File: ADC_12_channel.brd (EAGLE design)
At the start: 148.1 x 127 mm, 165 parts, among them IC1 LM317BD2T, IC2 LM317BD2T, K1 691131710003, K2 691101710002, K3 691101710002, K4 691101710002, K5 691101710002, K6 691101710002, K7 691101710002, K8 691101710002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

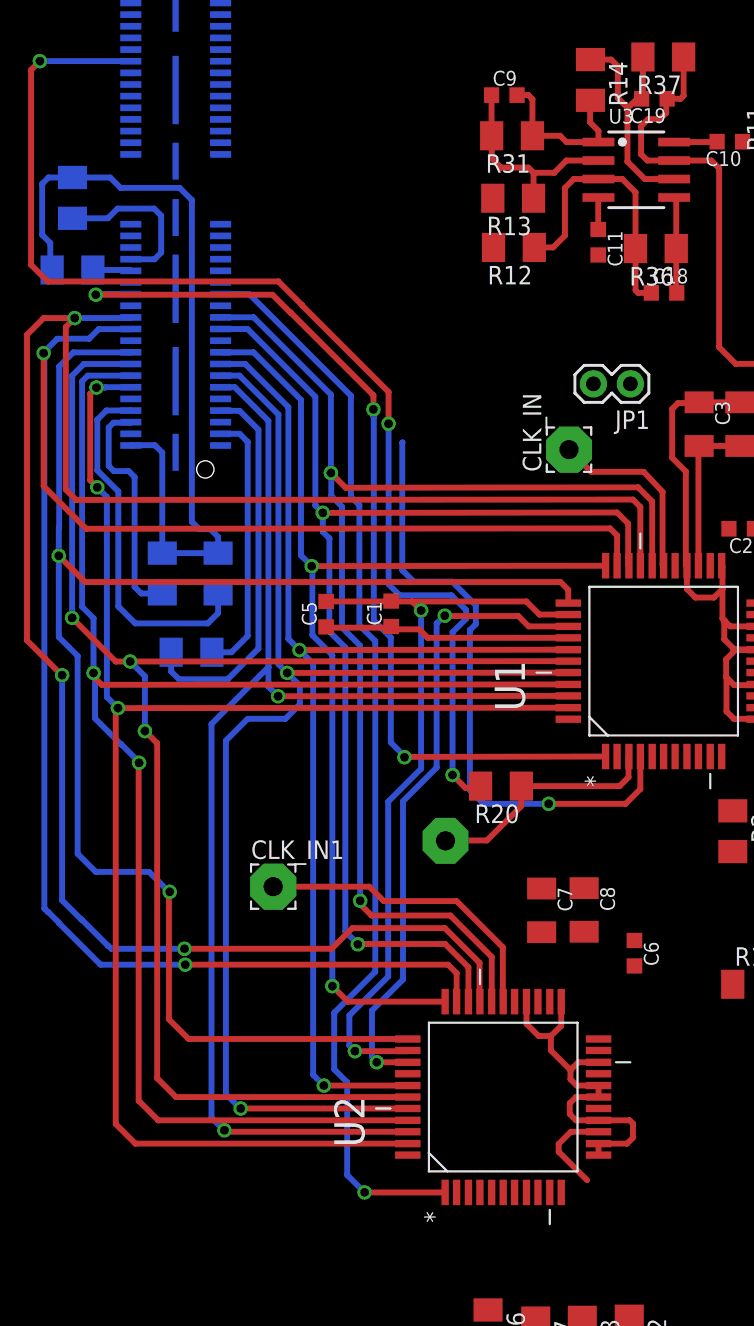
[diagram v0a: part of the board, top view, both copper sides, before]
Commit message: Finished connections to header
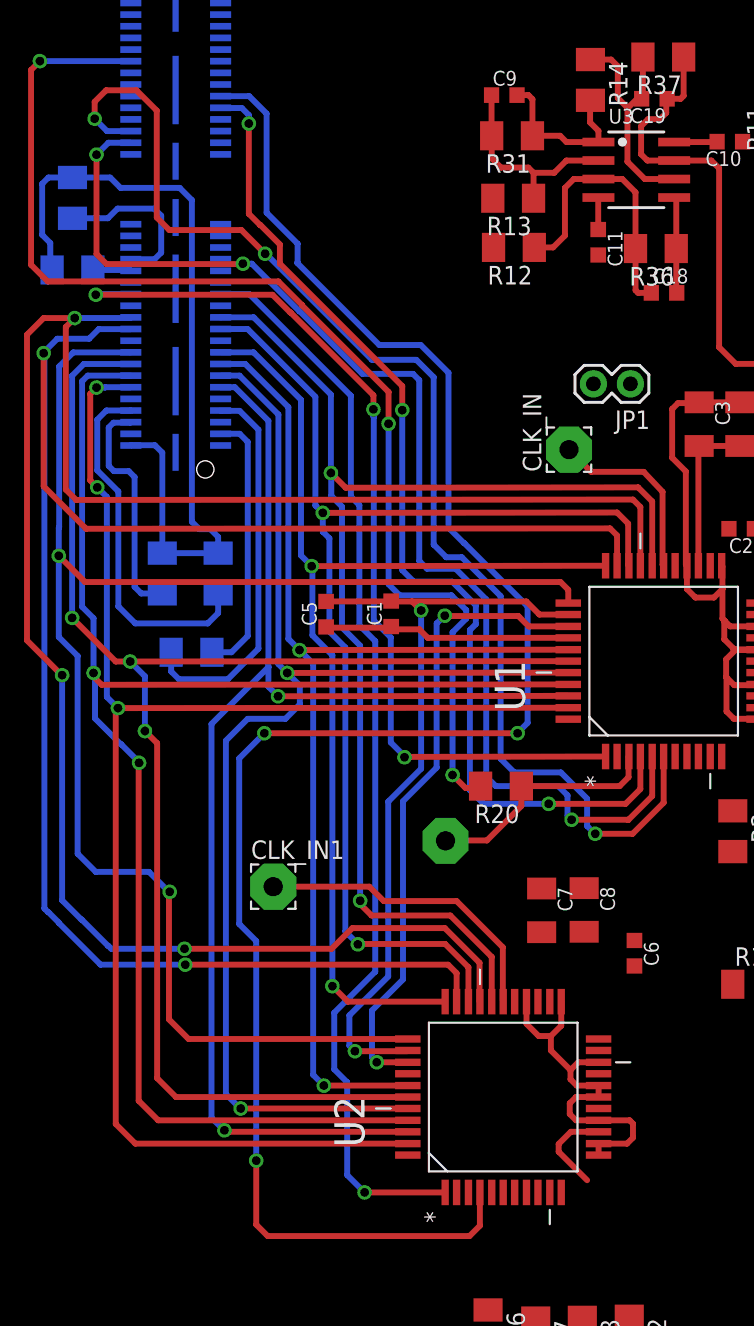
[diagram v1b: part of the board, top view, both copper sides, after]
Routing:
- net CS3N: track 0.00 -> 126.3 mm, vias 0 -> 3
- net WE: track 0.00 -> 87.3 mm, vias 0 -> 3
- net RD: track 0.00 -> 82.5 mm, vias 0 -> 3
- net CS2N: track 42.5 -> 71.5 mm, vias 1 -> 3
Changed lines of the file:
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@@
 <wire x1="29.1592" y1="23.8506" x2="26.5176" y2="23.8506" width="0.4064" layer="16"/>
 <wire x1="26.5176" y1="23.8506" x2="25.7302" y2="24.638" width="0.4064" layer="16"/>
-<wire x1="25.7302" y1="24.638" x2="25.7302" y2="33.401" width="0.4064" layer="16"/>
-<wire x1="25.7302" y1="33.401" x2="25.7556" y2="33.4264" width="0.4064" layer="16"/>
-<wire x1="25.7556" y1="33.4264" x2="13.25" y2="56.405" width="0" layer="19" extent="1-16"/>
+<wire x1="25.7302" y1="24.638" x2="25.7302" y2="35.6362" width="0.4064" layer="16"/>
+<via x="25.7302" y="35.6362" extent="1-16" drill="0.6"/>
+<wire x1="25.7302" y1="35.6362" x2="25.7302" y2="37.2872" width="0.4064" layer="1"/>
+<wire x1="25.7302" y1="37.2872" x2="17.3228" y2="45.6946" width="0.4064" layer="1"/>
+<wire x1="17.3228" y1="45.6946" x2="17.3228" y2="47.0154" width="0.4064" layer="1"/>
+<wire x1="17.3228" y1="47.0154" x2="15.9766" y2="48.3616" width="0.4064" layer="1"/>
+<wire x1="15.9766" y1="48.3616" x2="15.9512" y2="48.3616" width="0.4064" layer="1"/>
+<wire x1="15.9512" y1="48.3616" x2="15.1892" y2="49.1236" width="0.4064" layer="1"/>
+<wire x1="15.1892" y1="49.1236" x2="15.1892" y2="55.3212" width="0.4064" layer="1"/>
+<via x="15.1892" y="55.3212" extent="1-16" drill="0.6"/>
+<wire x1="15.1892" y1="55.3212" x2="15.1892" y2="55.9054" width="0.4064" layer="16"/>
+<wire x1="15.1892" y1="55.9054" x2="14.7066" y2="56.388" width="0.4064" layer="16"/>
+<wire x1="14.7066" y1="56.388" x2="13.267" y2="56.388" width="0.4064" layer="16"/>
+<wire x1="13.267" y1="56.388" x2="13.25" y2="56.405" width="0.4064" layer="16"/>
 </signal>
 <signal name="CS3N">
 <contactref element="U2" pad="4"/>
 <contactref element="X1" pad="51"/>
-<wire x1="31.0642" y1="-18.1102" x2="13.25" y2="57.205" width="0" layer="19" extent="1-16"/>
+<wire x1="31.0642" y1="-18.1102" x2="31.0642" y2="-20.3962" width="0.4064" layer="1"/>
+<wire x1="31.0642" y1="-20.3962" x2="30.353" y2="-21.1074" width="0.4064" layer="1"/>
+<wire x1="30.353" y1="-21.1074" x2="16.4846" y2="-21.1074" width="0.4064" layer="1"/>
+<wire x1="16.4846" y1="-21.1074" x2="15.6972" y2="-20.32" width="0.4064" layer="1"/>
+<wire x1="15.6972" y1="-20.32" x2="15.6972" y2="-15.9258" width="0.4064" layer="1"/>
+<via x="15.6972" y="-15.9258" extent="1-16" drill="0.6"/>
+<wire x1="15.6972" y1="-15.9258" x2="15.6972" y2="-0.8382" width="0.4064" layer="16"/>
+<wire x1="15.6972" y1="-0.8382" x2="14.5288" y2="0.3302" width="0.4064" layer="16"/>
+<wire x1="14.5288" y1="0.3302" x2="14.5288" y2="11.7094" width="0.4064" layer="16"/>
+<wire x1="14.5288" y1="11.7094" x2="16.256" y2="13.4366" width="0.4064" layer="16"/>
+<via x="16.256" y="13.4366" extent="1-16" drill="0.6"/>
+<wire x1="16.256" y1="13.4366" x2="33.655" y2="13.4366" width="0.4064" layer="1"/>
+<via x="33.655" y="13.4366" extent="1-16" drill="0.6"/>
+<wire x1="33.655" y1="13.4366" x2="33.655" y2="13.462" width="0.4064" layer="16"/>
+<wire x1="33.655" y1="13.462" x2="34.3408" y2="14.1478" width="0.4064" layer="16"/>
+<wire x1="34.3408" y1="14.1478" x2="34.3408" y2="22.1488" width="0.4064" layer="16"/>
+<wire x1="34.3408" y1="22.1488" x2="29.9974" y2="26.4922" width="0.4064" layer="16"/>
+<wire x1="29.9974" y1="26.4922" x2="29.972" y2="26.4922" width="0.4064" layer="16"/>
+<wire x1="29.972" y1="26.4922" x2="28.9052" y2="27.559" width="0.4064" layer="16"/>
+<wire x1="28.9052" y1="27.559" x2="28.9052" y2="38.2016" width="0.4064" layer="16"/>
+<wire x1="28.9052" y1="38.2016" x2="27.0002" y2="40.1066" width="0.4064" layer="16"/>
+<wire x1="27.0002" y1="40.1066" x2="24.1554" y2="40.1066" width="0.4064" layer="16"/>
+<wire x1="24.1554" y1="40.1066" x2="18.5166" y2="45.7454" width="0.4064" layer="16"/>
+<wire x1="13.25" y1="57.205" x2="15.2104" y2="57.205" width="0.4064" layer="16"/>
+<wire x1="15.2104" y1="57.205" x2="16.4084" y2="56.007" width="0.4064" layer="16"/>
+<wire x1="16.4084" y1="56.007" x2="16.4084" y2="49.1998" width="0.4064" layer="16"/>
+<wire x1="16.4084" y1="49.1998" x2="18.542" y2="47.0662" width="0.4064" layer="16"/>
+<wire x1="18.542" y1="47.0662" x2="18.542" y2="45.7708" width="0.4064" layer="16"/>
+<wire x1="18.542" y1="45.7708" x2="18.5166" y2="45.7454" width="0.4064" layer="16"/>
 </signal>
 <signal name="RD">
@@
 <contactref element="U1" pad="5"/>
 <contactref element="U2" pad="5"/>
-<wire x1="42.9006" y1="11.8364" x2="7.08" y2="54.005" width="0" layer="19" extent="1-16"/>
-<wire x1="31.877" y1="-18.1102" x2="42.9006" y2="11.8364" width="0" layer="19" extent="1-1"/>
+<wire x1="42.9006" y1="11.8364" x2="42.9006" y2="9.1186" width="0.4064" layer="1"/>
+<wire x1="42.9006" y1="9.1186" x2="41.2496" y2="7.4676" width="0.4064" layer="1"/>
+<wire x1="31.496" y1="10.4648" x2="31.496" y2="22.6314" width="0.4064" layer="16"/>
+<wire x1="31.496" y1="22.6314" x2="29.3878" y2="24.7396" width="0.4064" layer="16"/>
+<wire x1="7.08" y1="54.005" x2="5.5418" y2="54.005" width="0.4064" layer="16"/>
+<wire x1="5.5418" y1="54.005" x2="4.7244" y2="53.1876" width="0.4064" layer="16"/>
+<via x="4.7244" y="53.1876" extent="1-16" drill="0.6"/>
+<wire x1="4.7244" y1="53.1876" x2="4.7244" y2="46.355" width="0.4064" layer="1"/>
+<wire x1="4.7244" y1="46.355" x2="5.4102" y2="45.6692" width="0.4064" layer="1"/>
+<wire x1="5.4102" y1="45.6692" x2="14.7574" y2="45.6692" width="0.4064" layer="1"/>
+<wire x1="14.7574" y1="45.6692" x2="14.7828" y2="45.6946" width="0.4064" layer="1"/>
+<via x="14.7828" y="45.6946" extent="1-16" drill="0.6"/>
+<wire x1="14.7828" y1="45.6946" x2="15.3924" y2="45.6946" width="0.4064" layer="16"/>
+<wire x1="15.3924" y1="45.6946" x2="18.669" y2="42.418" width="0.4064" layer="16"/>
+<wire x1="18.669" y1="42.418" x2="18.6944" y2="42.418" width="0.4064" layer="16"/>
+<wire x1="18.6944" y1="42.418" x2="22.987" y2="38.1254" width="0.4064" layer="16"/>
+<wire x1="22.987" y1="38.1254" x2="26.4668" y2="38.1254" width="0.4064" layer="16"/>
+<wire x1="26.4668" y1="38.1254" x2="26.8986" y2="37.6936" width="0.4064" layer="16"/>
+<wire x1="26.8986" y1="37.6936" x2="26.8986" y2="25.273" width="0.4064" layer="16"/>
+<wire x1="26.8986" y1="25.273" x2="27.432" y2="24.7396" width="0.4064" layer="16"/>
+<wire x1="27.432" y1="24.7396" x2="29.3878" y2="24.7396" width="0.4064" layer="16"/>
+<wire x1="31.496" y1="10.4648" x2="32.1564" y2="9.8044" width="0.4064" layer="16"/>
+<wire x1="32.1564" y1="9.8044" x2="36.449" y2="9.8044" width="0.4064" layer="16"/>
+<wire x1="36.449" y1="9.8044" x2="37.084" y2="9.1694" width="0.4064" layer="16"/>
+<wire x1="37.084" y1="9.1694" x2="37.084" y2="7.7724" width="0.4064" layer="16"/>
+<wire x1="37.084" y1="7.7724" x2="37.3634" y2="7.493" width="0.4064" layer="16"/>
+<via x="37.3634" y="7.493" extent="1-16" drill="0.6"/>
+<wire x1="37.3634" y1="7.493" x2="41.2242" y2="7.493" width="0.4064" layer="1"/>
+<wire x1="41.2242" y1="7.493" x2="41.2496" y2="7.4676" width="0.4064" layer="1"/>
+<wire x1="31.877" y1="-18.1102" x2="37.3634" y2="7.493" width="0" layer="19" extent="1-1"/>
 </signal>
 <signal name="WE">
@@
 <contactref element="U2" pad="6"/>
 <contactref element="U1" pad="6"/>
-<wire x1="43.688" y1="11.8364" x2="7.08" y2="54.805" width="0" layer="19" extent="1-16"/>
-<wire x1="32.6644" y1="-18.1102" x2="43.688" y2="11.8364" width="0" layer="19" extent="1-1"/>
+<wire x1="7.08" y1="54.805" x2="5.4438" y2="54.805" width="0.4064" layer="16"/>
+<wire x1="5.4438" y1="54.805" x2="4.5974" y2="55.6514" width="0.4064" layer="16"/>
+<via x="4.5974" y="55.6514" extent="1-16" drill="0.6"/>
+<wire x1="4.5974" y1="55.6514" x2="4.5974" y2="56.8198" width="0.4064" layer="1"/>
+<wire x1="4.5974" y1="56.8198" x2="5.3848" y2="57.6072" width="0.4064" layer="1"/>
+<wire x1="5.3848" y1="57.6072" x2="7.4676" y2="57.6072" width="0.4064" layer="1"/>
+<wire x1="7.4676" y1="57.6072" x2="8.8646" y2="56.2102" width="0.4064" layer="1"/>
+<wire x1="43.688" y1="11.8364" x2="43.688" y2="8.6614" width="0.4064" layer="1"/>
+<wire x1="43.688" y1="8.6614" x2="41.5544" y2="6.5278" width="0.4064" layer="1"/>
+<wire x1="41.5544" y1="6.5278" x2="38.989" y2="6.5278" width="0.4064" layer="1"/>
+<via x="38.989" y="6.5278" extent="1-16" drill="0.6"/>
+<wire x1="38.989" y1="6.5278" x2="38.9636" y2="6.5278" width="0.4064" layer="16"/>
+<wire x1="38.9636" y1="6.5278" x2="38.4302" y2="7.0612" width="0.4064" layer="16"/>
+<wire x1="38.4302" y1="7.0612" x2="38.4302" y2="8.9408" width="0.4064" layer="16"/>
+<wire x1="38.4302" y1="8.9408" x2="36.6268" y2="10.7442" width="0.4064" layer="16"/>
+<wire x1="36.6268" y1="10.7442" x2="33.4264" y2="10.7442" width="0.4064" layer="16"/>
+<wire x1="33.4264" y1="10.7442" x2="32.4866" y2="11.684" width="0.4064" layer="16"/>
+<wire x1="32.4866" y1="11.684" x2="32.4866" y2="22.86" width="0.4064" layer="16"/>
+<wire x1="32.4866" y1="22.86" x2="29.8196" y2="25.527" width="0.4064" layer="16"/>
+<wire x1="29.8196" y1="25.527" x2="28.7528" y2="25.527" width="0.4064" layer="16"/>
+<wire x1="28.7528" y1="25.527" x2="27.8892" y2="26.3906" width="0.4064" layer="16"/>
+<wire x1="27.8892" y1="26.3906" x2="27.8892" y2="37.8968" width="0.4064" layer="16"/>
+<wire x1="27.8892" y1="37.8968" x2="26.6954" y2="39.0906" width="0.4064" layer="16"/>
+<wire x1="8.8646" y1="56.2102" x2="8.8646" y2="48.8696" width="0.4064" layer="1"/>
+<wire x1="8.8646" y1="48.8696" x2="9.7282" y2="48.006" width="0.4064" layer="1"/>
+<wire x1="9.7282" y1="48.006" x2="14.6812" y2="48.006" width="0.4064" layer="1"/>
+<wire x1="14.6812" y1="48.006" x2="16.3068" y2="46.3804" width="0.4064" layer="1"/>
+<via x="16.3068" y="46.3804" extent="1-16" drill="0.6"/>
+<wire x1="16.3068" y1="46.3804" x2="16.3576" y2="46.3804" width="0.4064" layer="16"/>
+<wire x1="16.3576" y1="46.3804" x2="23.6474" y2="39.0906" width="0.4064" layer="16"/>
+<wire x1="23.6474" y1="39.0906" x2="26.6954" y2="39.0906" width="0.4064" layer="16"/>
+<wire x1="32.6644" y1="-18.1102" x2="38.989" y2="6.5278" width="0" layer="19" extent="1-1"/>
 </signal>
 <signal name="CONVST">

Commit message: Connected ADC2 with header Relocated ADC2 towards right
came to know about the VDD DVDD issue! and missing of 5v supply,
will be resolved in next commit
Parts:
- moved R9 91.5 mm to (46.8, -22.5)
- moved JP1 56.4 mm to (53.2, -17.8)
- moved CONV_ST2 44.2 mm to (11.3, -17.4)
- moved R76 38.6 mm to (18.9, -17.6), turned to 90 degrees
- moved C7 29.6 mm to (64.4, -4.19)
- moved C6 21.5 mm to (63.2, -1.24)
- moved C8 18.5 mm to (56.1, -3.66)
- moved U2 4.52 mm to (37.2, -11.6)
- moved CONVST1 0.81 mm to (29.5, 6.05)
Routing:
- net RD: track 82.5 -> 135.2 mm, vias 3 -> 4
- net WE: track 87.3 -> 139.5 mm, vias 3 -> 4
- net CONVST: track 82.1 -> 116.3 mm, vias 3 -> 4
- net N$25: track 0.00 -> 26.2 mm, vias 0 -> 1
- net N$6: track 129.0 -> 133.6 mm
- net N$5: track 109.4 -> 113.9 mm
- net N$30: track 82.1 -> 86.6 mm
- net N$52: track 74.8 -> 79.4 mm
- net N$4: track 103.5 -> 108.0 mm
- net N$3: track 106.7 -> 111.2 mm
- net N$27: track 89.9 -> 94.4 mm
- net N$12: track 86.5 -> 91.1 mm
- net N$10: track 76.4 -> 81.0 mm
- net N$1: track 105.6 -> 110.1 mm
- net VCC_3+: track 43.8 -> 48.4 mm
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
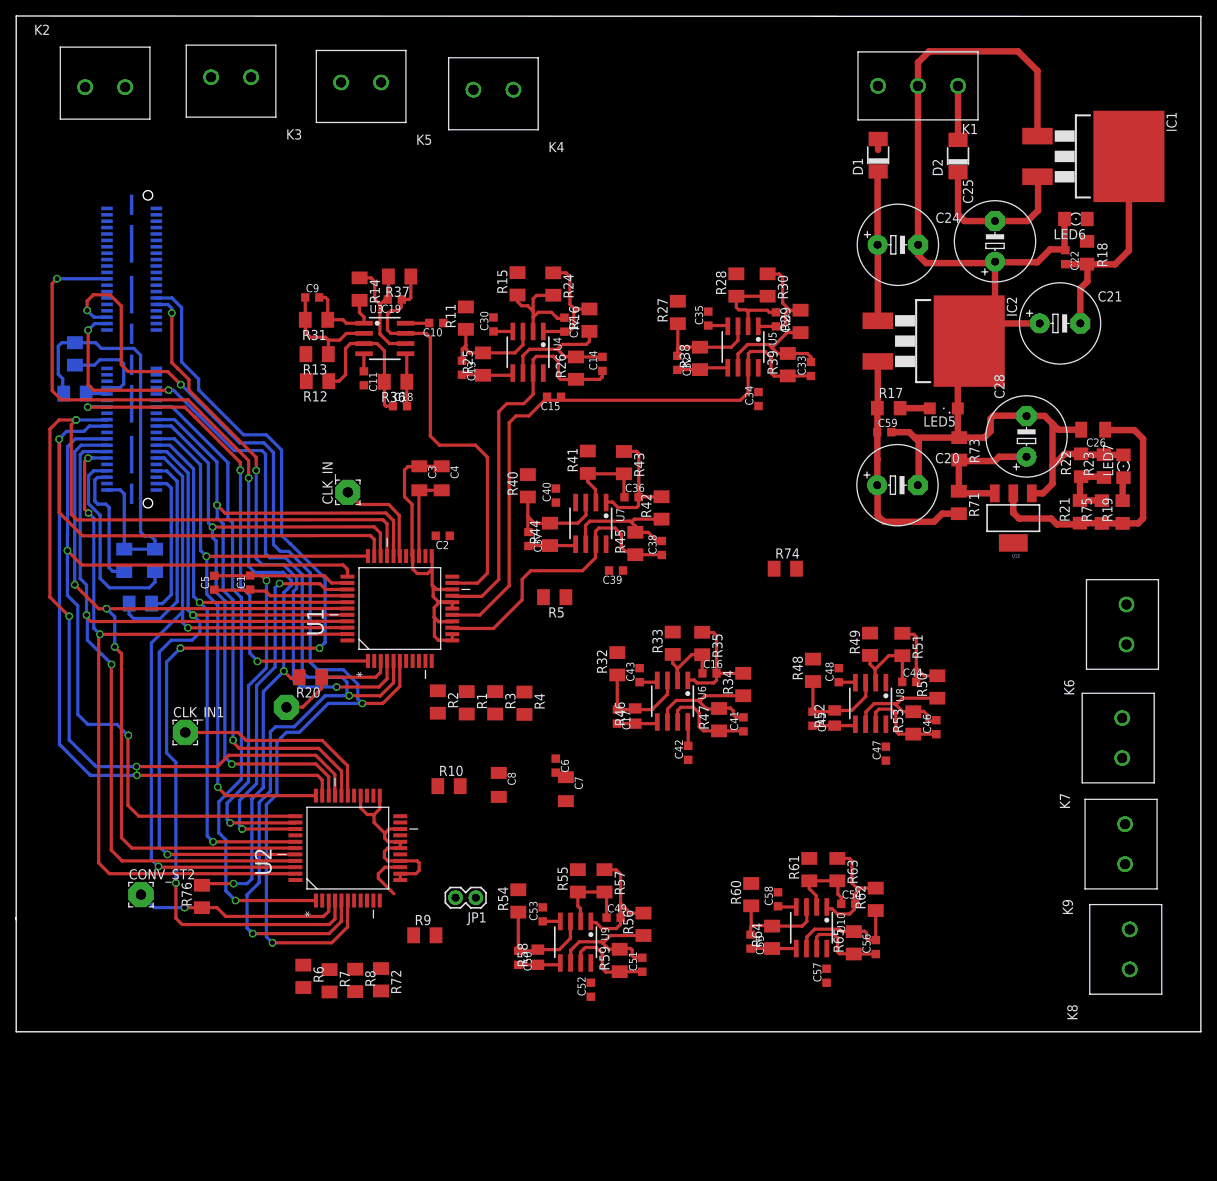
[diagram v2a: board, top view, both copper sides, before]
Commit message: Added 5v stage (for Vdd & DVdd)
Finally fixed the supply now. Only, taking out the 12v, 5v and 3v points remaining.
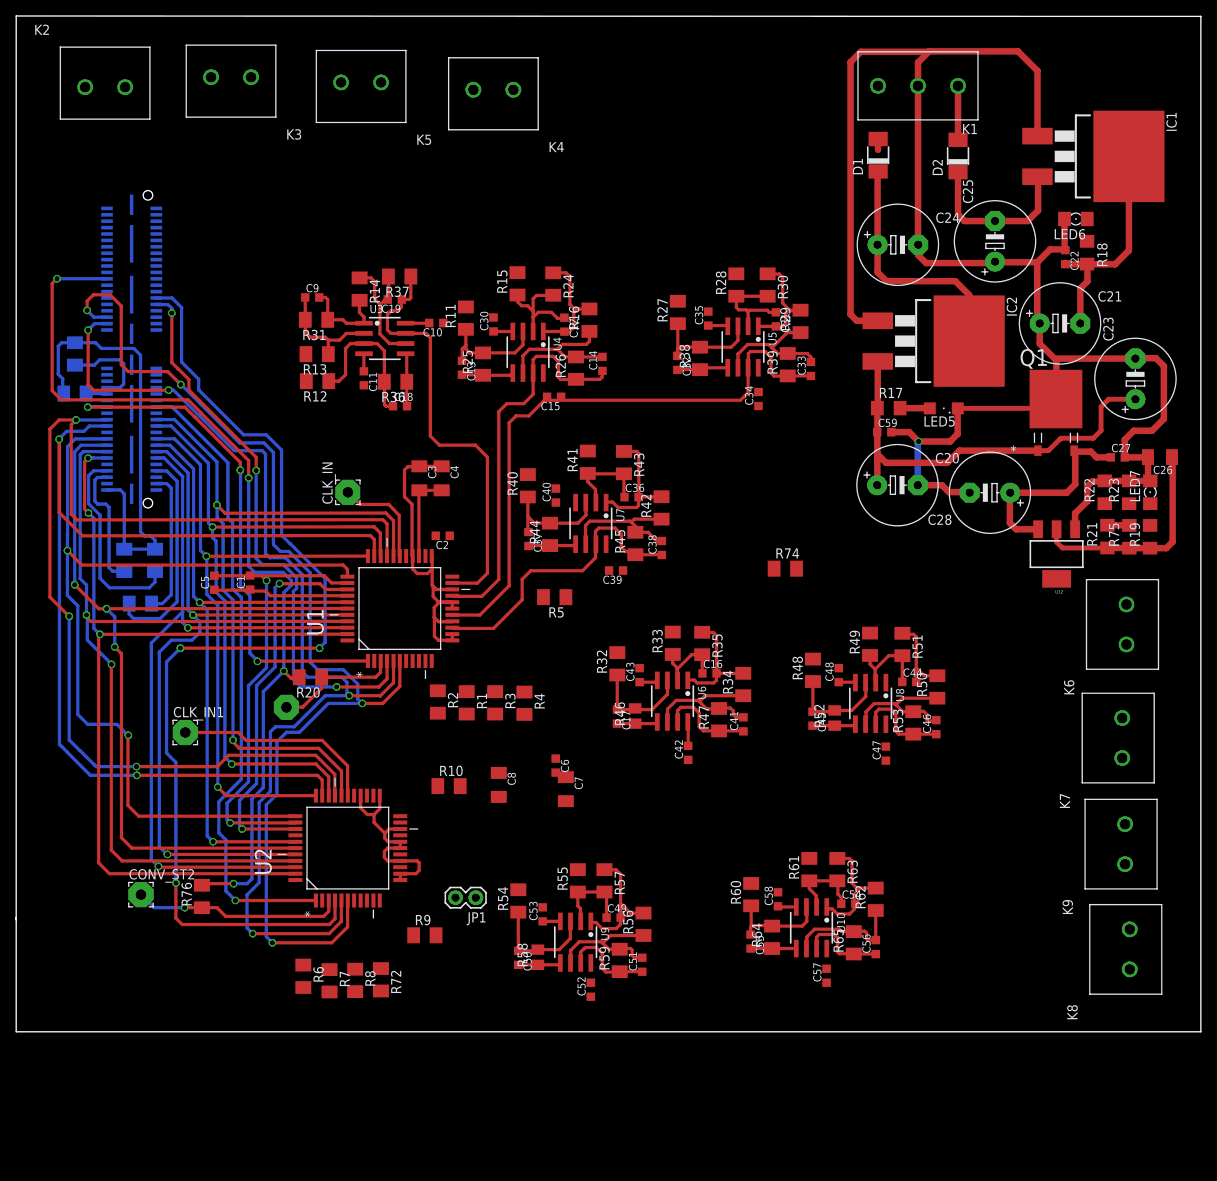
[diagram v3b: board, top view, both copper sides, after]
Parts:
- removed R71, R73: 0, resistor:M1206
- added C23: 1000uF/35V, rcl:E5-10,5
- added C27: 0.1u, rcl:C0603K
- added Q1: L78M12ABDT, ST Microelctronics_By_element14_Batch_1:TO225P972X240-3N
- moved C26 9.03 mm to (138.7, 37.3)
- moved C28 8.39 mm to (117.4, 32.9), turned to 180 degrees
- moved U12 7.03 mm to (125.8, 25.2)
- moved LED7 4.67 mm to (137.5, 32.9)
- moved R19 4.62 mm to (137.5, 27.4)
- moved R21 4.62 mm to (132.1, 27.4)
- moved R75 4.62 mm to (134.9, 27.4)
- moved R23 4.54 mm to (134.8, 32.9)
- moved R22 4.48 mm to (131.8, 32.9)
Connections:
- removed net 5V: C28.+, R71.1, R73.2, U12.3
- net DGND: now also C23.-, C27.2, IC2.1, Q1.2; no longer IC2.2, R73.1
- net N$36: now also IC2.2; no longer IC2.1
- net VCC_12+: now also C23.+, Q1.1; no longer R71.2
- net VDD: now also C27.1, C28.+, Q1.3, U12.3
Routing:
- net DGND: track 172.8 -> 240.7 mm, vias 0 -> 1
- net VDD: track 11.0 -> 36.5 mm
- net VCC_12+: track 36.2 -> 59.2 mm
- net 5V: track 17.2 -> 0.00 mm
- net N$36: track 18.7 -> 31.0 mm
- net VCC_5+: track 34.7 -> 27.4 mm
- net ADC8: track 18.2 -> 11.8 mm
- net 3V: track 8.68 -> 2.75 mm
- net N$41: track 2.91 -> 0.00 mm
